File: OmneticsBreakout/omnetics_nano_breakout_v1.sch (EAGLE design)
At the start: 2 parts

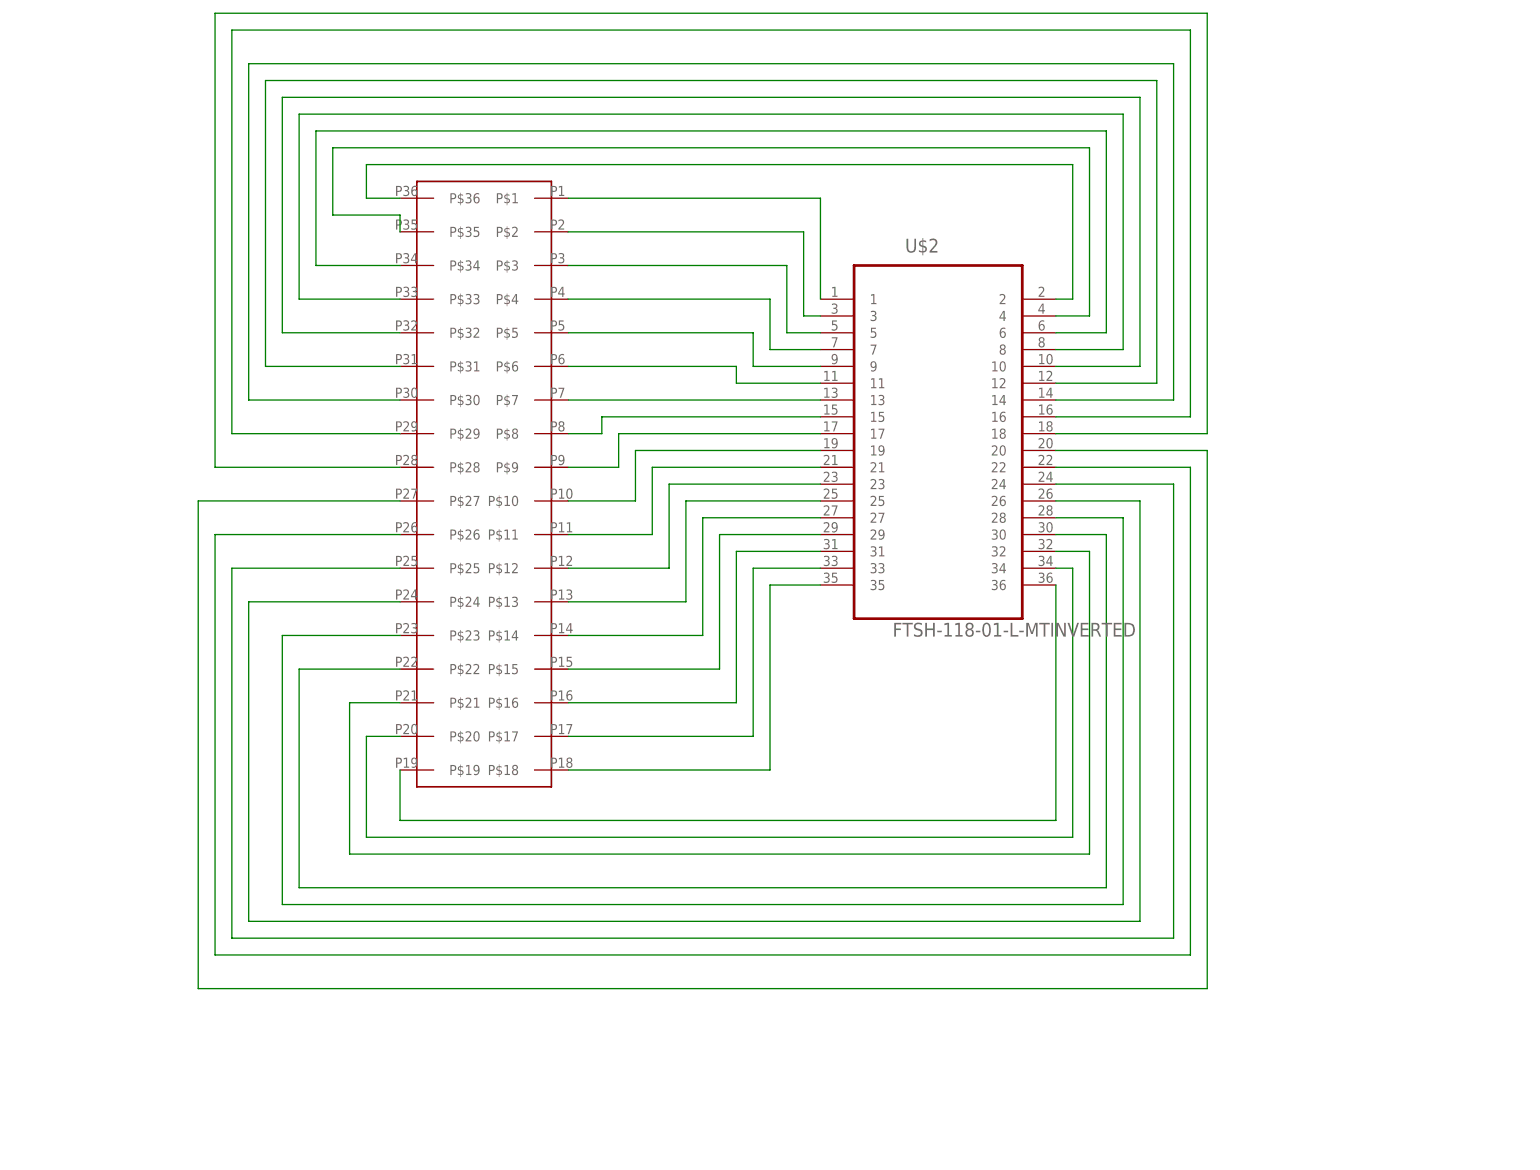
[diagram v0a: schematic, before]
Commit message: updated pinouts of omnetics board
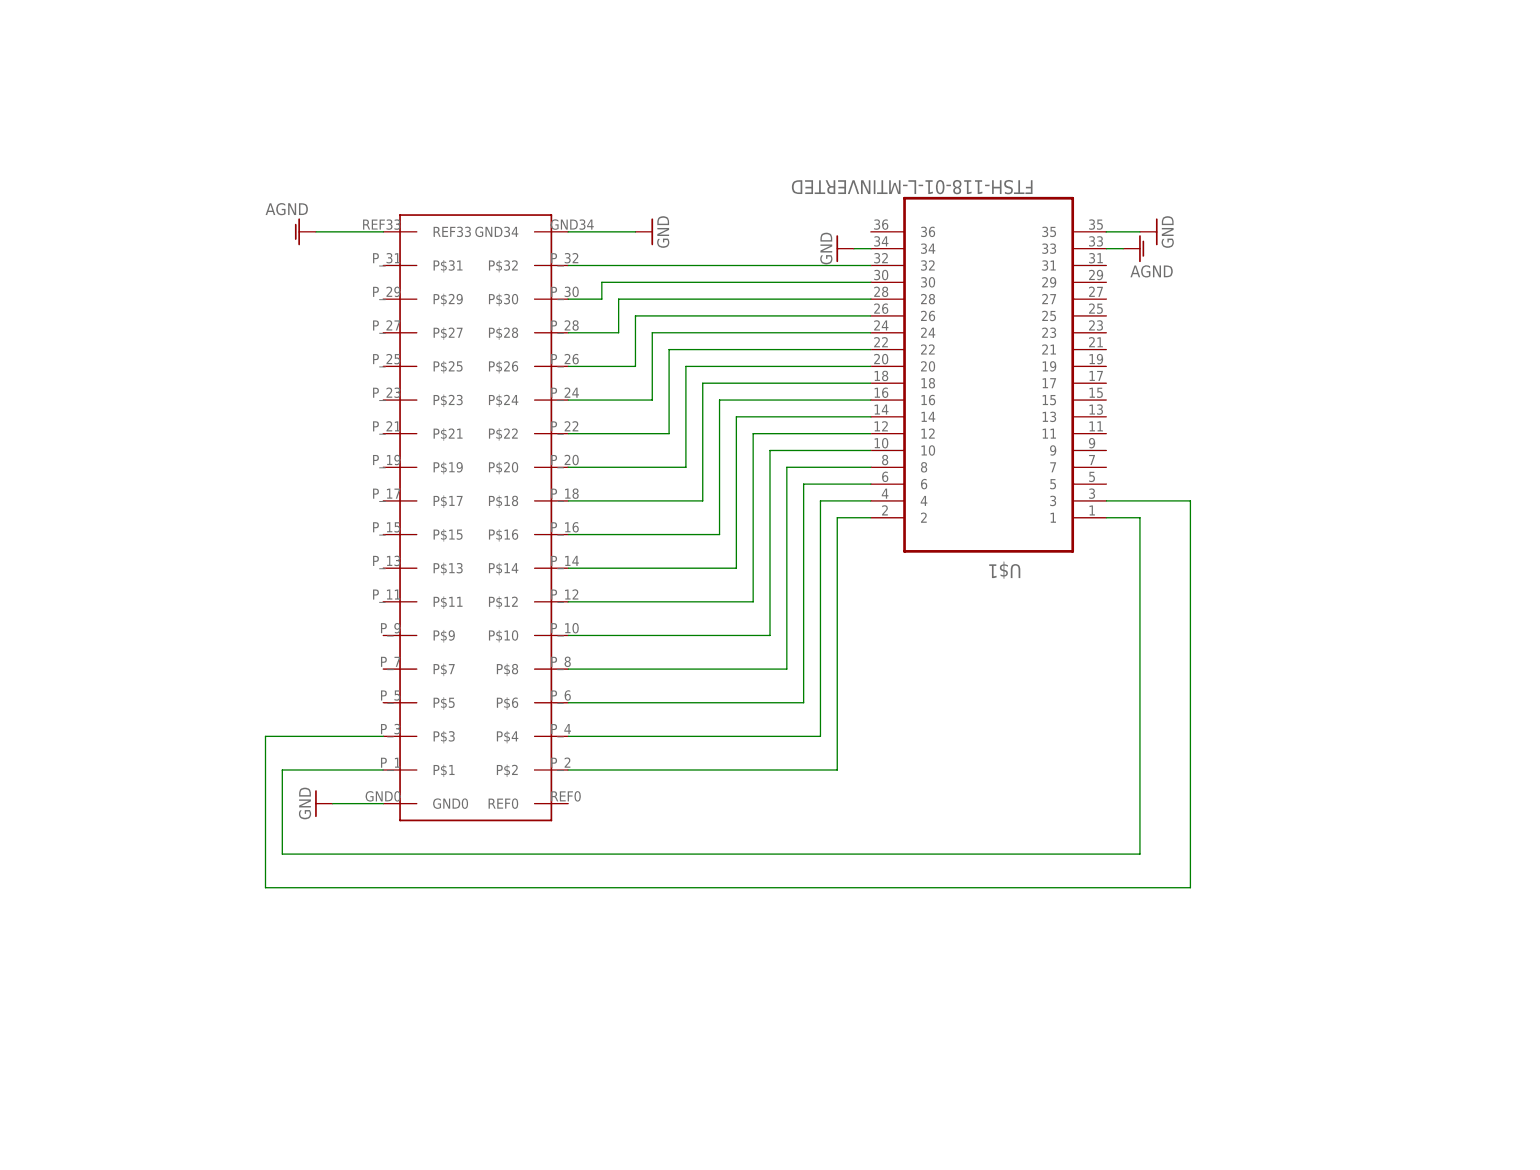
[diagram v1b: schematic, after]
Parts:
- U$1: value OMNETICS_NANO_18X2 -> FTSH-118-01-L-MTINVERTED; device Sombeck_lib:OMNETICS_NANO_18X2 -> tuckerLib:FTSH-118-01-L-MTINVERTED
- U$2: value FTSH-118-01-L-MTINVERTED -> OMNETICS_NANO_18X2; device tuckerLib:FTSH-118-01-L-MTINVERTED -> Sombeck_lib:OMNETICS_NANO_18X2
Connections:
- removed net N$19: U$1.P$36, U$2.2
- removed net N$20: U$1.P$35, U$2.4
- removed net N$21: U$1.P$34, U$2.6
- removed net N$22: U$1.P$33, U$2.8
- removed net N$23: U$1.P$32, U$2.10
- removed net N$24: U$1.P$31, U$2.12
- removed net N$25: U$1.P$30, U$2.14
- removed net N$26: U$1.P$29, U$2.16
- removed net N$27: U$1.P$28, U$2.18
- removed net N$28: U$1.P$19, U$2.36
- removed net N$29: U$1.P$20, U$2.34
- removed net N$30: U$1.P$21, U$2.32
- removed net N$31: U$1.P$22, U$2.30
- removed net N$32: U$1.P$23, U$2.28
- removed net N$33: U$1.P$24, U$2.26
- removed net N$34: U$1.P$25, U$2.24
- removed net N$35: U$1.P$26, U$2.22
- removed net N$36: U$1.P$27, U$2.20
- new net AGND: U$1.33, U$2.REF33
- new net GND: U$1.34, U$1.35, U$2.GND0, U$2.GND34
- net N$1: now also U$1.1, U$2.P$1; no longer U$1.P$1, U$2.1
- net N$10: now also U$1.18, U$2.P$18; no longer U$1.P$10, U$2.19
- net N$11: now also U$1.20, U$2.P$20; no longer U$1.P$11, U$2.21
- net N$12: now also U$1.22, U$2.P$22; no longer U$1.P$12, U$2.23
- net N$13: now also U$1.24, U$2.P$24; no longer U$1.P$13, U$2.25
- net N$14: now also U$1.26, U$2.P$26; no longer U$1.P$14, U$2.27
- net N$15: now also U$1.28, U$2.P$28; no longer U$1.P$15, U$2.29
- net N$16: now also U$1.30, U$2.P$30; no longer U$1.P$16, U$2.31
- net N$17: now also U$1.32, U$2.P$32; no longer U$1.P$17, U$2.33
- net N$18: now also U$1.3, U$2.P$3; no longer U$1.P$18, U$2.35
- net N$2: now also U$1.2, U$2.P$2; no longer U$1.P$2, U$2.3
- net N$3: now also U$1.4, U$2.P$4; no longer U$1.P$3, U$2.5
- net N$4: now also U$1.6, U$2.P$6; no longer U$1.P$4, U$2.7
- net N$5: now also U$1.8, U$2.P$8; no longer U$1.P$5, U$2.9
- net N$6: now also U$1.10, U$2.P$10; no longer U$1.P$6, U$2.11
- net N$7: now also U$1.12, U$2.P$12; no longer U$1.P$7, U$2.13
- net N$8: now also U$1.14, U$2.P$14; no longer U$1.P$8, U$2.15
- net N$9: now also U$1.16, U$2.P$16; no longer U$1.P$9, U$2.17

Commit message: omnetics breakout board update
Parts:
- removed U$1: FTSH-118-01-L-MTINVERTED, tuckerLib:FTSH-118-01-L-MTINVERTED
- added U$3: FTSH-118-01-L-MTREGULAR, tuckerLib:FTSH-118-01-L-MTREGULAR
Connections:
- new net N$19: U$2.P$5, U$3.5
- new net N$20: U$2.P$7, U$3.7
- new net N$21: U$2.P$9, U$3.9
- new net N$22: U$2.P$11, U$3.11
- new net N$23: U$2.P$13, U$3.13
- new net N$24: U$2.P$15, U$3.15
- new net N$25: U$2.P$17, U$3.17
- new net N$26: U$2.P$19, U$3.19
- new net N$27: U$2.P$21, U$3.21
- new net N$28: U$2.P$23, U$3.23
- new net N$29: U$2.P$25, U$3.25
- new net N$30: U$2.P$27, U$3.27
- new net N$31: U$2.P$29, U$3.29
- new net N$32: U$2.P$31, U$3.31
- net AGND: now also U$3.33; no longer U$1.33
- net GND: now also U$3.34, U$3.35; no longer U$1.34, U$1.35
- net N$1: now also U$3.1; no longer U$1.1
- net N$10: now also U$3.18; no longer U$1.18
- net N$11: now also U$3.20; no longer U$1.20
- net N$12: now also U$3.22; no longer U$1.22
- net N$13: now also U$3.24; no longer U$1.24
- net N$14: now also U$3.26; no longer U$1.26
- net N$15: now also U$3.28; no longer U$1.28
- net N$16: now also U$3.30; no longer U$1.30
- net N$17: now also U$3.32; no longer U$1.32
- net N$18: now also U$3.3; no longer U$1.3
- net N$2: now also U$3.2; no longer U$1.2
- net N$3: now also U$3.4; no longer U$1.4
- net N$4: now also U$3.6; no longer U$1.6
- net N$5: now also U$3.8; no longer U$1.8
- net N$6: now also U$3.10; no longer U$1.10
- net N$7: now also U$3.12; no longer U$1.12
- net N$8: now also U$3.14; no longer U$1.14
- net N$9: now also U$3.16; no longer U$1.16
